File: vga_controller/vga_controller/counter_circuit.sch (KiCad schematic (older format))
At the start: 7 parts, among them U1 74LS161, U2 74LS161, U3 74LS161, U4 74LS161, U5 74LS161, U6 74LS161, X1 ACO-xxxMHz

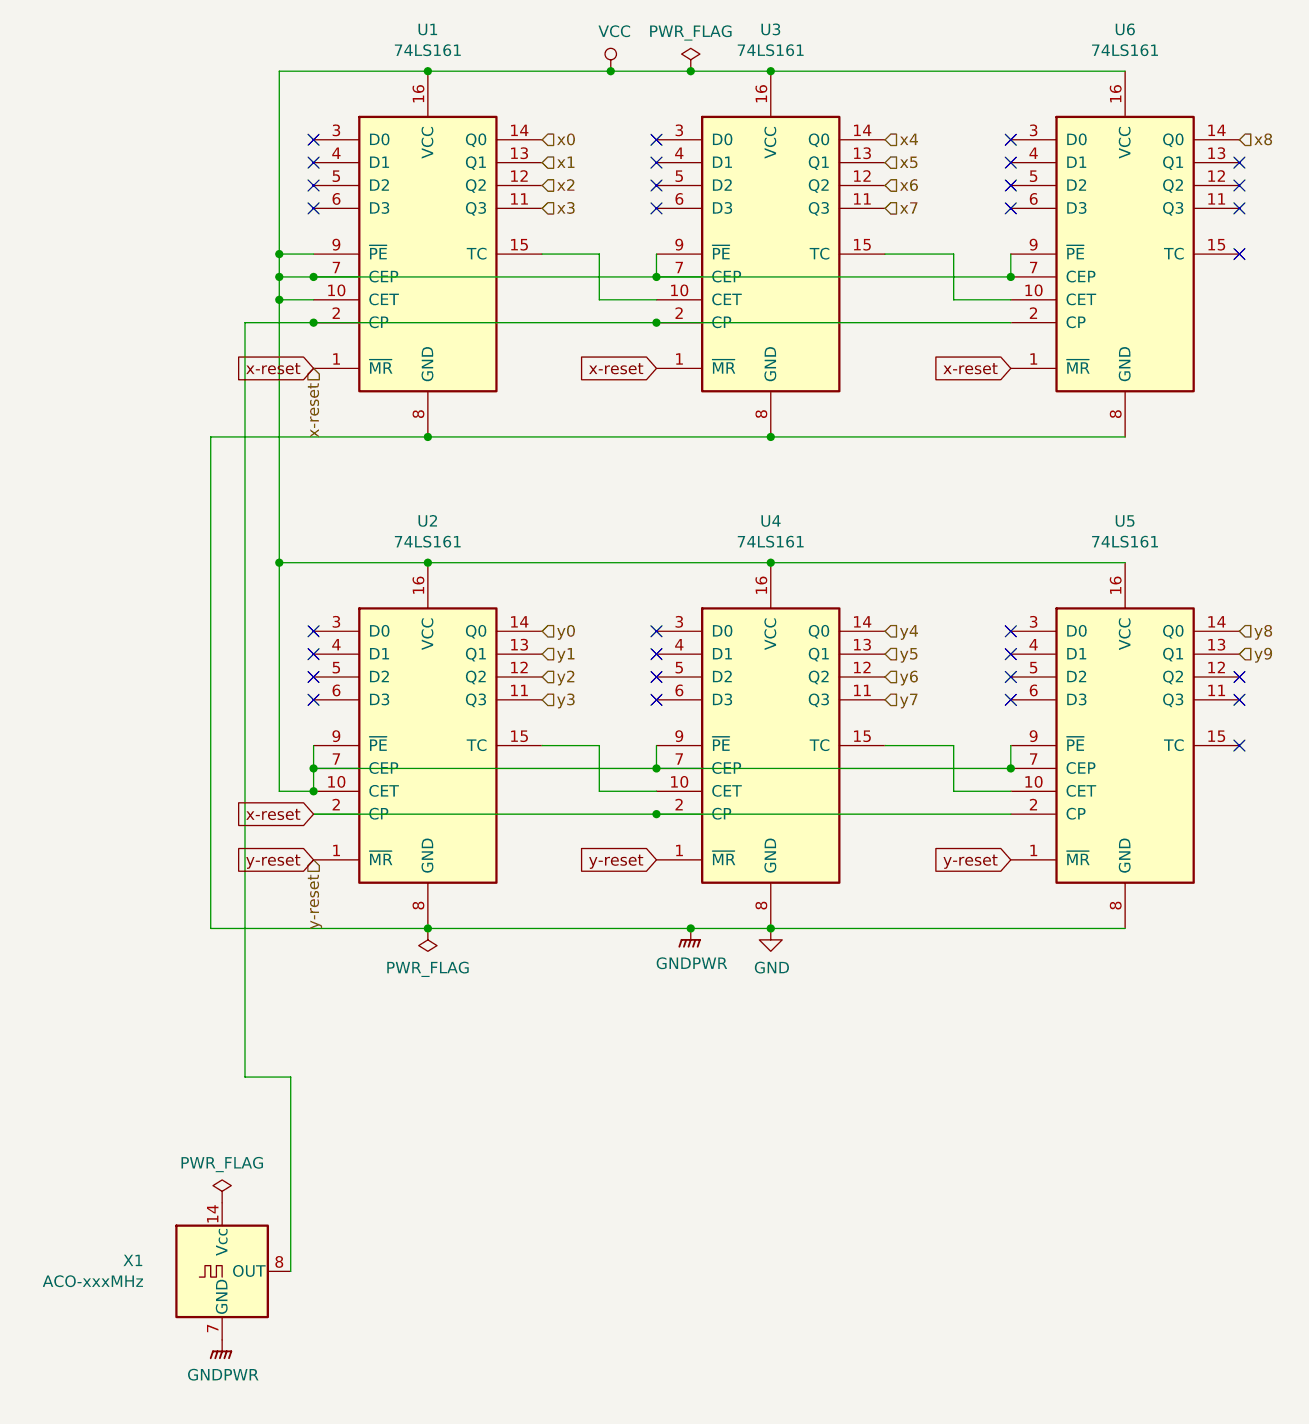
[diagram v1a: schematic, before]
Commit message: added correct labels, supressed errors
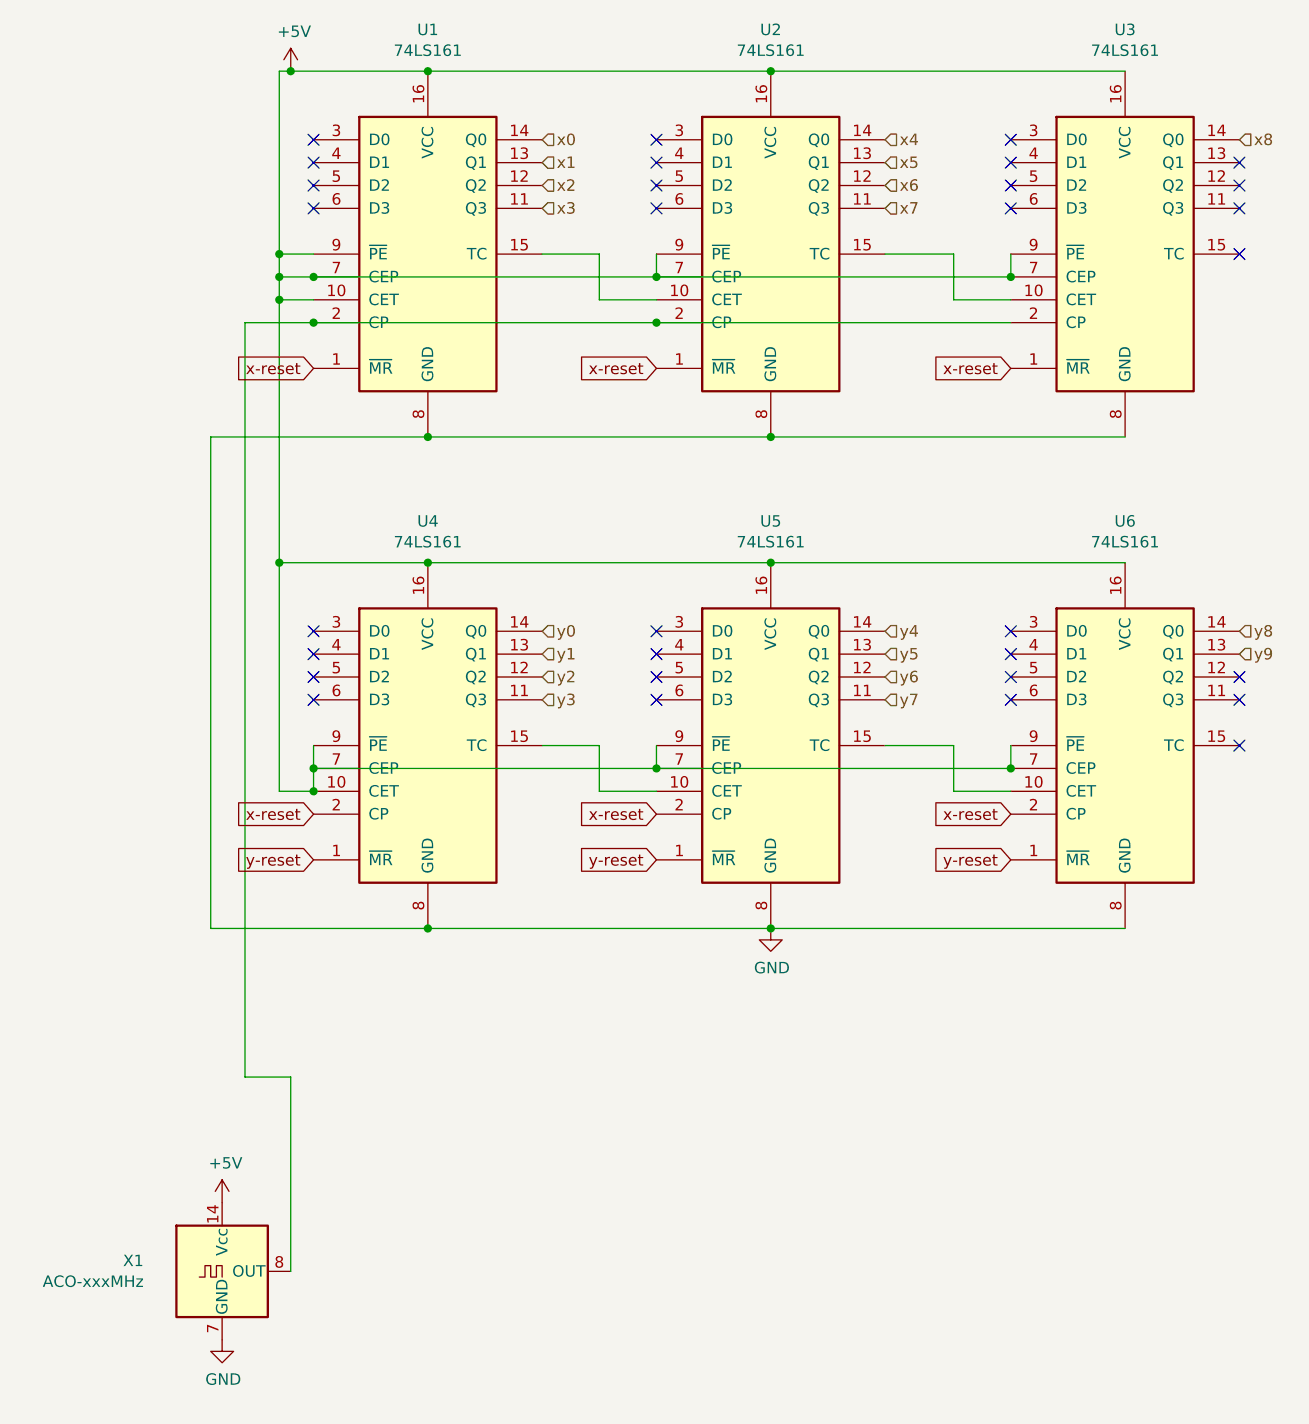
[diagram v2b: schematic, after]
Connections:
- net x-reset: now also U2.1 (~MR), U6.2 (CP); no longer U2.2 (CP), U6.1 (~MR)
- net x4: now also U2.14 (Q0); no longer U3.14 (Q0)
- net x5: now also U2.13 (Q1); no longer U3.13 (Q1)
- net x6: now also U2.12 (Q2); no longer U3.12 (Q2)
- net x7: now also U2.11 (Q3); no longer U3.11 (Q3)
- net x8: now also U3.14 (Q0); no longer U6.14 (Q0)
- net y-reset: now also U6.1 (~MR); no longer U2.1 (~MR)
- net y0: now also U4.14 (Q0); no longer U2.14 (Q0)
- net y1: now also U4.13 (Q1); no longer U2.13 (Q1)
- net y2: now also U4.12 (Q2); no longer U2.12 (Q2)
- net y3: now also U4.11 (Q3); no longer U2.11 (Q3)
- net y4: now also U5.14 (Q0); no longer U4.14 (Q0)
- net y5: now also U5.13 (Q1); no longer U4.13 (Q1)
- net y6: now also U5.12 (Q2); no longer U4.12 (Q2)
- net y7: now also U5.11 (Q3); no longer U4.11 (Q3)
- net y8: now also U6.14 (Q0); no longer U5.14 (Q0)
- net y9: now also U6.13 (Q1); no longer U5.13 (Q1)
- net +5V: now reaches X1.14 (Vcc)
- net +5V: now also U1.10 (CET), U1.16 (VCC), U1.7 (CEP), U1.9 (~PE), U2.16 (VCC), U2.7 (CEP), U2.9 (~PE), U3.16 (VCC), U3.7 (CEP), U3.9 (~PE), U4.10 (CET), U4.16 (VCC), U4.7 (CEP), U4.9 (~PE), U5.16 (VCC), U5.7 (CEP), U5.9 (~PE), U6.16 (VCC), U6.7 (CEP), U6.9 (~PE)
- net at U1.2 (CP), U3.2 (CP), X1.8 (OUT): now also U2.2 (CP); no longer U6.2 (CP)
- net at U5.15 (TC): now also U6.10 (CET)
- net at U2.15 (TC): now also U3.10 (CET); no longer U4.10 (CET)
- net at U3.15 (TC): no longer U6.10 (CET)
- net at U1.15 (TC): now also U2.10 (CET); no longer U3.10 (CET)
- removed net VCC: U1.10 (CET), U1.16 (VCC), U1.7 (CEP), U1.9 (~PE), U2.10 (CET), U2.16 (VCC), U2.7 (CEP), U2.9 (~PE), U3.16 (VCC), U3.7 (CEP), U3.9 (~PE), U4.16 (VCC), U4.7 (CEP), U4.9 (~PE), U5.16 (VCC), U5.7 (CEP), U5.9 (~PE), U6.16 (VCC), U6.7 (CEP), U6.9 (~PE)
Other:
- moved on the sheet: U2, U3, U4, U5, U6
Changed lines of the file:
@@
 $Descr A4 11693 8268
 encoding utf-8
-Sheet 2 5
-Title ""
+Sheet 5 5
+Title "counter circuit for VGA controller"
 Date ""
 Rev ""
-Comp ""
+Comp "Anirudha Chari"
 Comment1 ""
 Comment2 ""
@@
 Comment4 ""
 $EndDescr
-Connection ~ 2250 4800
 Connection ~ 2250 2650
 Wire Wire Line
-	1300 4800 2250 4800
-Wire Wire Line
 	1300 2650 1300 4800
 Wire Wire Line
 	2250 2650 1300 2650
-Wire Wire Line
-	3400 1050 3750 1050
-Connection ~ 3400 1050
-Wire Wire Line
-	2250 3200 3750 3200
-$Comp
-L power:PWR_FLAG #FLG02
-U 1 1 5E7F37F6
-P 3400 1050
-F 0 "#FLG02" H 3400 1125 50  0001 C CNN
-F 1 "PWR_FLAG" H 3400 1223 50  0000 C CNN
-F 2 "" H 3400 1050 50  0001 C CNN
-F 3 "~" H 3400 1050 50  0001 C CNN
-	1    3400 1050
-	1    0    0    -1
-$EndComp
-Wire Wire Line
-	3050 1050 3400 1050
-Connection ~ 3050 1050
-$Comp
-L power:VCC #PWR02
-U 1 1 5E7F37FE
-P 3050 1050
-F 0 "#PWR02" H 3050 900 50  0001 C CNN
-F 1 "VCC" H 3067 1223 50  0000 C CNN
-F 2 "" H 3050 1050 50  0001 C CNN
-F 3 "" H 3050 1050 50  0001 C CNN
-	1    3050 1050
-	1    0    0    -1
-$EndComp
 Wire Wire Line
 	1600 3200 1600 4200
 Connection ~ 1600 3200
-Connection ~ 2250 3200
 Wire Wire Line
 	1600 2050 1600 3200
-Wire Wire Line
-	2250 3200 1600 3200
-Wire Wire Line
-	3400 4800 3750 4800
-Connection ~ 3400 4800
-$Comp
-L power:GNDPWR #PWR03
-U 1 1 5E7F3812
-P 3400 4800
-F 0 "#PWR03" H 3400 4600 50  0001 C CNN
-F 1 "GNDPWR" H 3404 4646 50  0000 C CNN
-F 2 "" H 3400 4750 50  0001 C CNN
-F 3 "" H 3400 4750 50  0001 C CNN
-	1    3400 4800
-	1    0    0    -1
-$EndComp
 NoConn ~ 5800 3700
 NoConn ~ 5800 3800
@@
 Wire Wire Line
 	3250 4000 3250 4100
-Connection ~ 1750 4200
 Connection ~ 1750 4100
 Wire Wire Line
@@
 	1600 1050 1600 1850
 Wire Wire Line
-	2250 1050 1600 1050
+	2250 1050 1650 1050
 NoConn ~ 4800 3800
 NoConn ~ 4800 3700
@@
 Wire Wire Line
 	1750 2150 1450 2150
-Connection ~ 3250 4300
-Wire Wire Line
-	4800 4300 3250 4300
-Wire Wire Line
-	1750 4300 3250 4300
 Wire Wire Line
 	3250 2150 1750 2150
@@
 	3750 3200 5300 3200
 Connection ~ 3750 3200
-Wire Wire Line
-	2250 1050 3050 1050
 Connection ~ 3750 4800
 Wire Wire Line
 	5300 4800 3750 4800
 Wire Wire Line
-	2250 4800 3400 4800
-Wire Wire Line
 	2250 2650 3750 2650
-$Comp
-L power:GNDPWR #PWR01
-U 1 1 5E7F388F
-P 1350 6600
-F 0 "#PWR01" H 1350 6400 50  0001 C CNN
-F 1 "GNDPWR" H 1354 6446 50  0000 C CNN
-F 2 "" H 1350 6550 50  0001 C CNN
-F 3 "" H 1350 6550 50  0001 C CNN
-	1    1350 6600
-	1    0    0    -1
-$EndComp
-$Comp
-L power:PWR_FLAG #FLG01
-U 1 1 5E7F3895
-P 1350 6000
-F 0 "#FLG01" H 1350 6075 50  0001 C CNN
-F 1 "PWR_FLAG" H 1350 6173 50  0000 C CNN
-F 2 "" H 1350 6000 50  0001 C CNN
-F 3 "~" H 1350 6000 50  0001 C CNN
-	1    1350 6000
-	1    0    0    -1
-$EndComp
 $Comp
 L 74xx:74LS161 U5
 U 1 1 5E7F38A1
-P 5300 4000
-F 0 "U5" H 5300 4981 50  0000 C CNN
-F 1 "74LS161" H 5300 4890 50  0000 C CNN
-F 2 "" H 5300 4000 50  0001 C CNN
-F 3 "http://www.ti.com/lit/gpn/sn74LS161" H 5300 4000 50  0001 C CNN
-	1    5300 4000
-	1    0    0    -1
-$EndComp
-$Comp
-L 74xx:74LS161 U4
-U 1 1 5E7F38A7
 P 3750 4000
-F 0 "U4" H 3750 4981 50  0000 C CNN
+F 0 "U5" H 3750 4981 50  0000 C CNN
 F 1 "74LS161" H 3750 4890 50  0000 C CNN
 F 2 "" H 3750 4000 50  0001 C CNN
@@
 L 74xx:74LS161 U2
 U 1 1 5E7F38B3
-P 2250 4000
-F 0 "U2" H 2250 4981 50  0000 C CNN
-F 1 "74LS161" H 2250 4890 50  0000 C CNN
-F 2 "" H 2250 4000 50  0001 C CNN
-F 3 "http://www.ti.com/lit/gpn/sn74LS161" H 2250 4000 50  0001 C CNN
-	1    2250 4000
-	1    0    0    -1
-$EndComp
-$Comp
-L 74xx:74LS161 U3
-U 1 1 5E7F38B9
 P 3750 1850
-F 0 "U3" H 3750 2831 50  0000 C CNN
+F 0 "U2" H 3750 2831 50  0000 C CNN
 F 1 "74LS161" H 3750 2740 50  0000 C CNN
 F 2 "" H 3750 1850 50  0001 C CNN
 F 3 "http://www.ti.com/lit/gpn/sn74LS161" H 3750 1850 50  0001 C CNN
 	1    3750 1850
+	1    0    0    -1
+$EndComp
+$Comp
+L 74xx:74LS161 U3
+U 1 1 5E7F38B9
+P 5300 1850
+F 0 "U3" H 5300 2831 50  0000 C CNN
+F 1 "74LS161" H 5300 2740 50  0000 C CNN
+F 2 "" H 5300 1850 50  0001 C CNN
+F 3 "http://www.ti.com/lit/gpn/sn74LS161" H 5300 1850 50  0001 C CNN
+	1    5300 1850
 	1    0    0    -1
 $EndComp
@@
 F 3 "http://www.ti.com/lit/gpn/sn74LS161" H 2250 1850 50  0001 C CNN
 	1    2250 1850
-	1    0    0    -1
-$EndComp
-$Comp
-L power:GND #PWR04
-U 1 1 5E7F3809
-P 3750 4800
-F 0 "#PWR04" H 3750 4550 50  0001 C CNN
-F 1 "GND" H 3755 4627 50  0000 C CNN
-F 2 "" H 3750 4800 50  0001 C CNN
-F 3 "" H 3750 4800 50  0001 C CNN
-	1    3750 4800
 	1    0    0    -1
 $EndComp
@@
 L 74xx:74LS161 U6
 U 1 1 5E7F38AD
-P 5300 1850
-F 0 "U6" H 5300 2831 50  0000 C CNN
-F 1 "74LS161" H 5300 2740 50  0000 C CNN
-F 2 "" H 5300 1850 50  0001 C CNN
-F 3 "http://www.ti.com/lit/gpn/sn74LS161" H 5300 1850 50  0001 C CNN
-	1    5300 1850
+P 5300 4000
+F 0 "U6" H 5300 4981 50  0000 C CNN
+F 1 "74LS161" H 5300 4890 50  0000 C CNN
+F 2 "" H 5300 4000 50  0001 C CNN
+F 3 "http://www.ti.com/lit/gpn/sn74LS161" H 5300 4000 50  0001 C CNN
+	1    5300 4000
 	1    0    0    -1
 $EndComp
@@
 	1    0    0    -1
 $EndComp
-Text GLabel 4800 2350 0    50   Input ~ 0
-x-reset
-Text GLabel 3250 2350 0    50   Input ~ 0
-x-reset
+Text GLabel 1750 4500 0    50   Input ~ 0
+y-reset
+Text GLabel 1750 4300 0    50   Input ~ 0
+x-reset
+Text HLabel 5800 3600 2    50   Input ~ 0
+y9
+Text HLabel 5800 3500 2    50   Input ~ 0
+y8
+Text HLabel 4250 3800 2    50   Input ~ 0
+y7
+Text HLabel 4250 3700 2    50   Input ~ 0
+y6
+Text HLabel 4250 3600 2    50   Input ~ 0
+y5
+Text HLabel 4250 3500 2    50   Input ~ 0
+y4
+Text HLabel 2750 3800 2    50   Input ~ 0
+y3
+Text HLabel 2750 3700 2    50   Input ~ 0
+y2
+Text HLabel 2750 3600 2    50   Input ~ 0
+y1
+Text HLabel 2750 3500 2    50   Input ~ 0
+y0
+Text HLabel 5800 1350 2    50   Input ~ 0
+x8
+Text HLabel 4250 1650 2    50   Input ~ 0
+x7
+Text HLabel 4250 1550 2    50   Input ~ 0
+x6
+Text HLabel 4250 1450 2    50   Input ~ 0
+x5
+Text HLabel 4250 1350 2    50   Input ~ 0
+x4
+Text HLabel 2750 1650 2    50   Input ~ 0
+x3
+Text HLabel 2750 1550 2    50   Input ~ 0
+x2
+Text HLabel 2750 1450 2    50   Input ~ 0
+x1
+Text HLabel 2750 1350 2    50   Input ~ 0
+x0
 Text GLabel 1750 2350 0    50   Input ~ 0
 x-reset
+Wire Wire Line
+	2250 1050 3750 1050
+Text GLabel 3250 4500 0    50   Input ~ 0
+y-reset
 Text GLabel 4800 4500 0    50   Input ~ 0
 y-reset
-Text GLabel 3250 4500 0    50   Input ~ 0
-y-reset
-Text GLabel 1750 4500 0    50   Input ~ 0
-y-reset
-Text HLabel 2750 1350 2    50   Input ~ 0
-x0
-Text HLabel 2750 1450 2    50   Input ~ 0
-x1
-Text HLabel 2750 1550 2    50   Input ~ 0
-x2
-Text HLabel 2750 1650 2    50   Input ~ 0
-x3
-Text HLabel 4250 1350 2    50   Input ~ 0
-x4
-Text HLabel 4250 1450 2    50   Input ~ 0
-x5
-Text HLabel 4250 1550 2    50   Input ~ 0
-x6
-Text HLabel 4250 1650 2    50   Input ~ 0
-x7
-Text HLabel 5800 1350 2    50   Input ~ 0
-x8
-Text HLabel 2750 3500 2    50   Input ~ 0
-y0
-Text HLabel 2750 3600 2    50   Input ~ 0
-y1
-Text HLabel 2750 3700 2    50   Input ~ 0
-y2
-Text HLabel 2750 3800 2    50   Input ~ 0
-y3
-Text HLabel 4250 3500 2    50   Input ~ 0
-y4
-Text HLabel 4250 3600 2    50   Input ~ 0
-y5
-Text HLabel 4250 3700 2    50   Input ~ 0
-y6
-Text HLabel 4250 3800 2    50   Input ~ 0
-y7
-Text HLabel 5800 3500 2    50   Input ~ 0
-y8
-Text HLabel 5800 3600 2    50   Input ~ 0
-y9
-Text GLabel 1750 4300 0    50   Input ~ 0
-x-reset
-Text HLabel 1750 2350 3    50   Input ~ 0
-x-reset
-Text HLabel 1750 4500 3    50   Input ~ 0
-y-reset
-$Comp
-L power:PWR_FLAG #FLG0101
-U 1 1 5E7407BD
-P 2250 4800
-F 0 "#FLG0101" H 2250 4875 50  0001 C CNN
-F 1 "PWR_FLAG" H 2250 4973 50  0000 C CNN
-F 2 "" H 2250 4800 50  0001 C CNN
-F 3 "~" H 2250 4800 50  0001 C CNN
-	1    2250 4800
-	-1   0    0    1
+Text GLabel 3250 4300 0    50   Input ~ 0
+x-reset
+Text GLabel 4800 4300 0    50   Input ~ 0
+x-reset
+Text GLabel 3250 2350 0    50   Input ~ 0
+x-reset
+Text GLabel 4800 2350 0    50   Input ~ 0
+x-reset
+Wire Wire Line
+	2250 4800 3750 4800
+Wire Wire Line
+	1300 4800 2250 4800
+Connection ~ 2250 4800
+Wire Wire Line
+	2250 3200 1600 3200
+Wire Wire Line
+	2250 3200 3750 3200
+Connection ~ 2250 3200
+Connection ~ 1750 4200
+$Comp
+L 74xx:74LS161 U4
+U 1 1 5E7F38A7
+P 2250 4000
+F 0 "U4" H 2250 4981 50  0000 C CNN
+F 1 "74LS161" H 2250 4890 50  0000 C CNN
+F 2 "" H 2250 4000 50  0001 C CNN
+F 3 "http://www.ti.com/lit/gpn/sn74LS161" H 2250 4000 50  0001 C CNN
+	1    2250 4000
+	1    0    0    -1
+$EndComp
+$Comp
+L power:+5V #PWR0101
+U 1 1 5E7720A1
+P 1650 1050
+F 0 "#PWR0101" H 1650 900 50  0001 C CNN
+F 1 "+5V" H 1665 1223 50  0000 C CNN
+F 2 "" H 1650 1050 50  0001 C CNN
+F 3 "" H 1650 1050 50  0001 C CNN
+	1    1650 1050
+	1    0    0    -1
+$EndComp
+Connection ~ 1650 1050
+Wire Wire Line
+	1650 1050 1600 1050
+$Comp
+L power:GND #PWR0103
+U 1 1 5E7722F4
+P 3750 4800
+F 0 "#PWR0103" H 3750 4550 50  0001 C CNN
+F 1 "GND" H 3755 4627 50  0000 C CNN
+F 2 "" H 3750 4800 50  0001 C CNN
+F 3 "" H 3750 4800 50  0001 C CNN
+	1    3750 4800
+	1    0    0    -1
+$EndComp
+$Comp
+L power:GND #PWR0104
+U 1 1 5E7724F2
+P 1350 6600
+F 0 "#PWR0104" H 1350 6350 50  0001 C CNN
+F 1 "GND" H 1355 6427 50  0000 C CNN
+F 2 "" H 1350 6600 50  0001 C CNN
+F 3 "" H 1350 6600 50  0001 C CNN
+	1    1350 6600
+	1    0    0    -1
+$EndComp
+$Comp
+L power:+5V #PWR0102
+U 1 1 5E772B4E
+P 1350 6000
+F 0 "#PWR0102" H 1350 5850 50  0001 C CNN
+F 1 "+5V" H 1365 6173 50  0000 C CNN
+F 2 "" H 1350 6000 50  0001 C CNN
+F 3 "" H 1350 6000 50  0001 C CNN
+	1    1350 6000
+	1    0    0    -1
 $EndComp
 $EndSCHEMATC

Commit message: made interconnects
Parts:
- renumbered U6 to U10, U1 to U5, U4 to U6, U2 to U7, U5 to U8, U3 to U9
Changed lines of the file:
@@
 	2250 2650 3750 2650
 $Comp
-L 74xx:74LS161 U5
+L 74xx:74LS161 U8
 U 1 1 5E7F38A1
 P 3750 4000
-F 0 "U5" H 3750 4981 50  0000 C CNN
+F 0 "U8" H 3750 4981 50  0000 C CNN
 F 1 "74LS161" H 3750 4890 50  0000 C CNN
 F 2 "" H 3750 4000 50  0001 C CNN
@@
 $EndComp
 $Comp
-L 74xx:74LS161 U2
+L 74xx:74LS161 U7
 U 1 1 5E7F38B3
 P 3750 1850
-F 0 "U2" H 3750 2831 50  0000 C CNN
+F 0 "U7" H 3750 2831 50  0000 C CNN
 F 1 "74LS161" H 3750 2740 50  0000 C CNN
 F 2 "" H 3750 1850 50  0001 C CNN
@@
 $EndComp
 $Comp
-L 74xx:74LS161 U3
+L 74xx:74LS161 U9
 U 1 1 5E7F38B9
 P 5300 1850
-F 0 "U3" H 5300 2831 50  0000 C CNN
+F 0 "U9" H 5300 2831 50  0000 C CNN
 F 1 "74LS161" H 5300 2740 50  0000 C CNN
 F 2 "" H 5300 1850 50  0001 C CNN
@@
 $EndComp
 $Comp
-L 74xx:74LS161 U1
+L 74xx:74LS161 U5
 U 1 1 5E7F38BF
 P 2250 1850
-F 0 "U1" H 2250 2831 50  0000 C CNN
+F 0 "U5" H 2250 2831 50  0000 C CNN
 F 1 "74LS161" H 2250 2740 50  0000 C CNN
 F 2 "" H 2250 1850 50  0001 C CNN
@@
 Connection ~ 4800 1950
 $Comp
-L 74xx:74LS161 U6
+L 74xx:74LS161 U10
 U 1 1 5E7F38AD
 P 5300 4000
-F 0 "U6" H 5300 4981 50  0000 C CNN
+F 0 "U10" H 5300 4981 50  0000 C CNN
 F 1 "74LS161" H 5300 4890 50  0000 C CNN
 F 2 "" H 5300 4000 50  0001 C CNN
@@
 Connection ~ 1750 4200
 $Comp
-L 74xx:74LS161 U4
+L 74xx:74LS161 U6
 U 1 1 5E7F38A7
 P 2250 4000
-F 0 "U4" H 2250 4981 50  0000 C CNN
+F 0 "U6" H 2250 4981 50  0000 C CNN
 F 1 "74LS161" H 2250 4890 50  0000 C CNN
 F 2 "" H 2250 4000 50  0001 C CNN
@@
 $EndComp
 $Comp
-L power:+5V #PWR0101
+L power:+5V #PWR012
 U 1 1 5E7720A1
 P 1650 1050
-F 0 "#PWR0101" H 1650 900 50  0001 C CNN
+F 0 "#PWR012" H 1650 900 50  0001 C CNN
 F 1 "+5V" H 1665 1223 50  0000 C CNN
 F 2 "" H 1650 1050 50  0001 C CNN
@@
 	1650 1050 1600 1050
 $Comp
-L power:GND #PWR0103
+L power:GND #PWR013
 U 1 1 5E7722F4
 P 3750 4800
-F 0 "#PWR0103" H 3750 4550 50  0001 C CNN
+F 0 "#PWR013" H 3750 4550 50  0001 C CNN
 F 1 "GND" H 3755 4627 50  0000 C CNN
 F 2 "" H 3750 4800 50  0001 C CNN
@@
 $EndComp
 $Comp
-L power:GND #PWR0104
+L power:GND #PWR011
 U 1 1 5E7724F2
 P 1350 6600
-F 0 "#PWR0104" H 1350 6350 50  0001 C CNN
+F 0 "#PWR011" H 1350 6350 50  0001 C CNN
 F 1 "GND" H 1355 6427 50  0000 C CNN
 F 2 "" H 1350 6600 50  0001 C CNN
@@
 $EndComp
 $Comp
-L power:+5V #PWR0102
+L power:+5V #PWR010
 U 1 1 5E772B4E
 P 1350 6000
-F 0 "#PWR0102" H 1350 5850 50  0001 C CNN
+F 0 "#PWR010" H 1350 5850 50  0001 C CNN
 F 1 "+5V" H 1365 6173 50  0000 C CNN
 F 2 "" H 1350 6000 50  0001 C CNN
